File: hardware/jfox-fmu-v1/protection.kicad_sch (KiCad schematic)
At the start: 12 parts, among them U40 USBLC6-2SC6

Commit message: Mezzanine to the carrier, microSD on the edge, sensors moved clear
Three placement changes, and the third is now measured rather than asserted.

QUICK ASSEMBLY. Ten JST-GH headers become one 60-way 0.5 mm mezzanine
(DF12C3.0-60DS) to the carrier, which is what ARCHITECTURE.md already argued
for: eleven looms is eleven things to make, inspect and vibrate loose.
Grounds are interleaved between signal groups rather than grouped at one end,
because a 60-pin connector with no local return is the worst discontinuity on
a board.

What deliberately does NOT cross it: the isolated CAN. A 0.5 mm pitch gives
about 0.5 mm of creepage between adjacent contacts, so running CAN1_H/L
alongside board-referenced signals would quietly reduce the isolation barrier
to that gap - which defeats the ISOW1044 entirely. CAN keeps dedicated
connectors on the isolated side. Debug, USB and the card slot also stay on the
module, because they are used at the module: putting them on the carrier means
unbolting the aircraft to read a log.

The three ferrites became one. Every harness now leaves through the mezzanine,
so there is one 5 V feed to filter instead of three - and three ferrites
driving nets nothing connects to is worse than none.

MICROSD ON THE EDGE, aligned by COURTYARD rather than origin. The first
attempt placed it by its origin and hung a 15 mm deep socket off the board.
The card now ejects outward, off the board, not into U10.

SENSORS MOVED, and the reason checked. The mezzanine freed ten headers' worth
of edge, so the sensors get a dedicated island in the bottom-left - the corner
furthest from both the buck at top-left and the isolated converters at
top-right. The magnetometer is placed by hand in the far corner rather than
packed, because DO-160G s15 makes it the most placement-sensitive part here.

check_fmu_placement.py measures it. "Keep the sensors away from the noise" is
obviously right, impossible to argue with, and untestable as written. Each
sensitive part now has a mini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
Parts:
- removed FB2, FB3: 600R@100MHz, Inductor_SMD:L_0805_2012Metric, symbol Device:FerriteBead
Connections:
- net +5V_TELEM renamed +5V_CARRIER
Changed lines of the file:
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@@
 		(instances
 			(project "jfox-fmu"
-				(path "/009937f3-12d8-4eba-91f7-a35ebf6e45f6"
+				(path "/7ec73105-955f-464d-bc9a-bc93cbe93b7f"
 					(reference "D4")
 					(unit 1)
@@
 		(instances
 			(project "jfox-fmu"
-				(path "/009937f3-12d8-4eba-91f7-a35ebf6e45f6"
+				(path "/7ec73105-955f-464d-bc9a-bc93cbe93b7f"
 					(reference "D5")
 					(unit 1)
@@
 		(instances
 			(project "jfox-fmu"
-				(path "/009937f3-12d8-4eba-91f7-a35ebf6e45f6"
+				(path "/7ec73105-955f-464d-bc9a-bc93cbe93b7f"
 					(reference "D6")
 					(unit 1)
@@
 		(instances
 			(project "jfox-fmu"
-				(path "/009937f3-12d8-4eba-91f7-a35ebf6e45f6"
+				(path "/7ec73105-955f-464d-bc9a-bc93cbe93b7f"
 					(reference "U40")
 					(unit 1)
@@
 		(instances
 			(project "jfox-fmu"
-				(path "/009937f3-12d8-4eba-91f7-a35ebf6e45f6"
+				(path "/7ec73105-955f-464d-bc9a-bc93cbe93b7f"
 					(reference "L5")
 					(unit 1)
@@
 		(instances
 			(project "jfox-fmu"
-				(path "/009937f3-12d8-4eba-91f7-a35ebf6e45f6"
+				(path "/7ec73105-955f-464d-bc9a-bc93cbe93b7f"
 					(reference "L3")
 					(unit 1)
@@
 		(instances
 			(project "jfox-fmu"
-				(path "/009937f3-12d8-4eba-91f7-a35ebf6e45f6"
+				(path "/7ec73105-955f-464d-bc9a-bc93cbe93b7f"
 					(reference "D7")
 					(unit 1)
@@
 		(instances
 			(project "jfox-fmu"
-				(path "/009937f3-12d8-4eba-91f7-a35ebf6e45f6"
+				(path "/7ec73105-955f-464d-bc9a-bc93cbe93b7f"
 					(reference "L4")
 					(unit 1)
@@
 		(instances
 			(project "jfox-fmu"
-				(path "/009937f3-12d8-4eba-91f7-a35ebf6e45f6"
+				(path "/7ec73105-955f-464d-bc9a-bc93cbe93b7f"
 					(reference "D8")
 					(unit 1)
@@
 		(instances
 			(project "jfox-fmu"
-				(path "/009937f3-12d8-4eba-91f7-a35ebf6e45f6"
+				(path "/7ec73105-955f-464d-bc9a-bc93cbe93b7f"
 					(reference "FB1")
 					(unit 1)
@@
 		)
 	)
-	(global_label "+5V_TELEM"
+	(global_label "+5V_CARRIER"
 		(shape input)
 		(at 58.42 138.43 180)
 		(fields_autoplaced yes)
 		(effects
-			(font
-				(size 1.27 1.27)
-			)
-			(justify left)
-		)
-	)
-	(symbol
-		(lib_id "Device:FerriteBead")
-		(at 104.14 130.81 0)
-		(unit 1)
-		(exclude_from_sim no)(in_bom yes)(on_board yes)(dnp no)
-		(property "Reference" "FB2"
-			(at 104.14 119.38 0)
-			(effects
-			(font
-				(size 1.27 1.27)
-			)
-		)
-		)
-		(property "Value" "600R@100MHz"
-			(at 104.14 142.24 0)
-			(effects
-			(font
-				(size 1.27 1.27)
-			)
-		)
-		)
-		(property "Footprint" "Inductor_SMD:L_0805_2012Metric"
-			(at 104.14 130.81 0)
-			(hide yes)
-			(effects
-			(font
-				(size 1.27 1.27)
-			)
-		)
-		)
-		(instances
-			(project "jfox-fmu"
-				(path "/009937f3-12d8-4eba-91f7-a35ebf6e45f6"
-					(reference "FB2")
-					(unit 1)
-				)
-			)
-		)
-	)
-	(wire
-		(pts
-			(xy 104.14 127.0) (xy 104.14 123.19)
-		)
-		(stroke
-			(width 0)
-			(type default)
-		)
-	)
-	(global_label "+5V"
-		(shape input)
-		(at 104.14 123.19 180)
-		(fields_autoplaced yes)
-		(effects
-			(font
-				(size 1.27 1.27)
-			)
-			(justify left)
-		)
-	)
-	(wire
-		(pts
-			(xy 104.14 134.62) (xy 104.14 138.43)
-		)
-		(stroke
-			(width 0)
-			(type default)
-		)
-	)
-	(global_label "+5V_GPS"
-		(shape input)
-		(at 104.14 138.43 180)
-		(fields_autoplaced yes)
-		(effects
-			(font
-				(size 1.27 1.27)
-			)
-			(justify left)
-		)
-	)
-	(symbol
-		(lib_id "Device:FerriteBead")
-		(at 149.86 130.81 0)
-		(unit 1)
-		(exclude_from_sim no)(in_bom yes)(on_board yes)(dnp no)
-		(property "Reference" "FB3"
-			(at 149.86 119.38 0)
-			(effects
-			(font
-				(size 1.27 1.27)
-			)
-		)
-		)
-		(property "Value" "600R@100MHz"
-			(at 149.86 142.24 0)
-			(effects
-			(font
-				(size 1.27 1.27)
-			)
-		)
-		)
-		(property "Footprint" "Inductor_SMD:L_0805_2012Metric"
-			(at 149.86 130.81 0)
-			(hide yes)
-			(effects
-			(font
-				(size 1.27 1.27)
-			)
-		)
-		)
-		(instances
-			(project "jfox-fmu"
-				(path "/009937f3-12d8-4eba-91f7-a35ebf6e45f6"
-					(reference "FB3")
-					(unit 1)
-				)
-			)
-		)
-	)
-	(wire
-		(pts
-			(xy 149.86 127.0) (xy 149.86 123.19)
-		)
-		(stroke
-			(width 0)
-			(type default)
-		)
-	)
-	(global_label "+5V"
-		(shape input)
-		(at 149.86 123.19 180)
-		(fields_autoplaced yes)
-		(effects
-			(font
-				(size 1.27 1.27)
-			)
-			(justify left)
-		)
-	)
-	(wire
-		(pts
-			(xy 149.86 134.62) (xy 149.86 138.43)
-		)
-		(stroke
-			(width 0)
-			(type default)
-		)
-	)
-	(global_label "+5V_RC"
-		(shape input)
-		(at 149.86 138.43 180)
-		(fields_autoplaced yes)
-		(effects

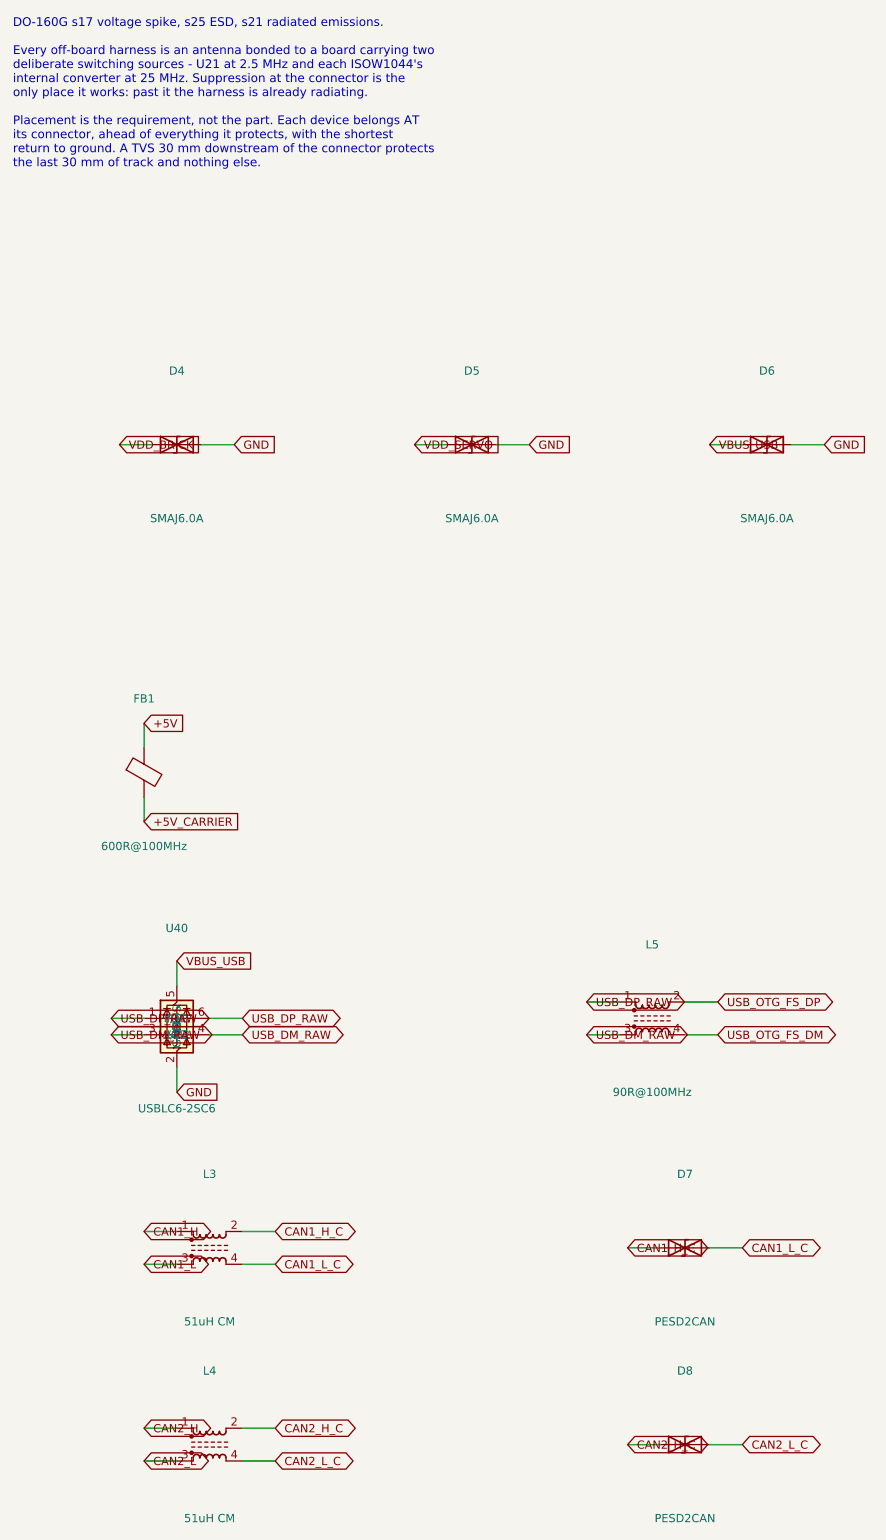
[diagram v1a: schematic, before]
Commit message: Card-cage TMR: FCU becomes a plug-in card, backplane carries the I/O
The FMU stops being a module that mates face-to-face with a base board
underneath it and becomes a card that slides into a backplane. That change
came from the JFOX FCU V1 sketch, and it dissolved a constraint I had
worked around rather than removed: the DF12 mezzanine's 3.0 mm stack height
joins two adjacent boards only, so three channels each needing an
independent path to one base board could not use it. Riser cards were the
workaround. Mating at the card's rear edge means nothing has to span the
gap, so the risers and their extra mated pair per channel are gone.

FCU card, 40 x 90 mm (was 100 x 80):
  * 58-contact Samtec MECF-30 card edge, polarised. Contacts 21/22 are a
    1.24 x 7.0 mm key notch offset from centre - a card the wrong way round
    physically will not enter, which is the only insertion safeguard that
    works before power is applied. Two grounds were sacrificed for it out of
    twenty rather than any signal.
  * Power input tree (LTC4417, six ORing FETs, dividers, input TVS) and the
    debug header move to the backplane. The card receives an already-ORed,
    already-fused +5V_CARRIER on three fingers.
  * Front edge carries everything a person touches: microSD, USB-C, and two
    lamps flanking it. D1 is hardwired to the rail so it lights with no
    firmware running - a power lamp the MCU drives tells you the MCU is
    alive, which is not what anyone reads it for.
  * Power and isolated blocks moved to the back face. Both noise groups are
    grouped at one end so the sensor island can sit 22 mm clear at the
    other; spread out, every point on an 80 mm body is within 13 mm of
    something switching.

JFOX-BASE-v1 backplane, 100 x 100 mm, new:
  * Three independent card-edge sockets in a column. A bent contact in one
    slot costs one channel; a shared bus would cost all three and leave the
    voter nothing to vote on.
  * Two airframe feeds at opposite corners, ORed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
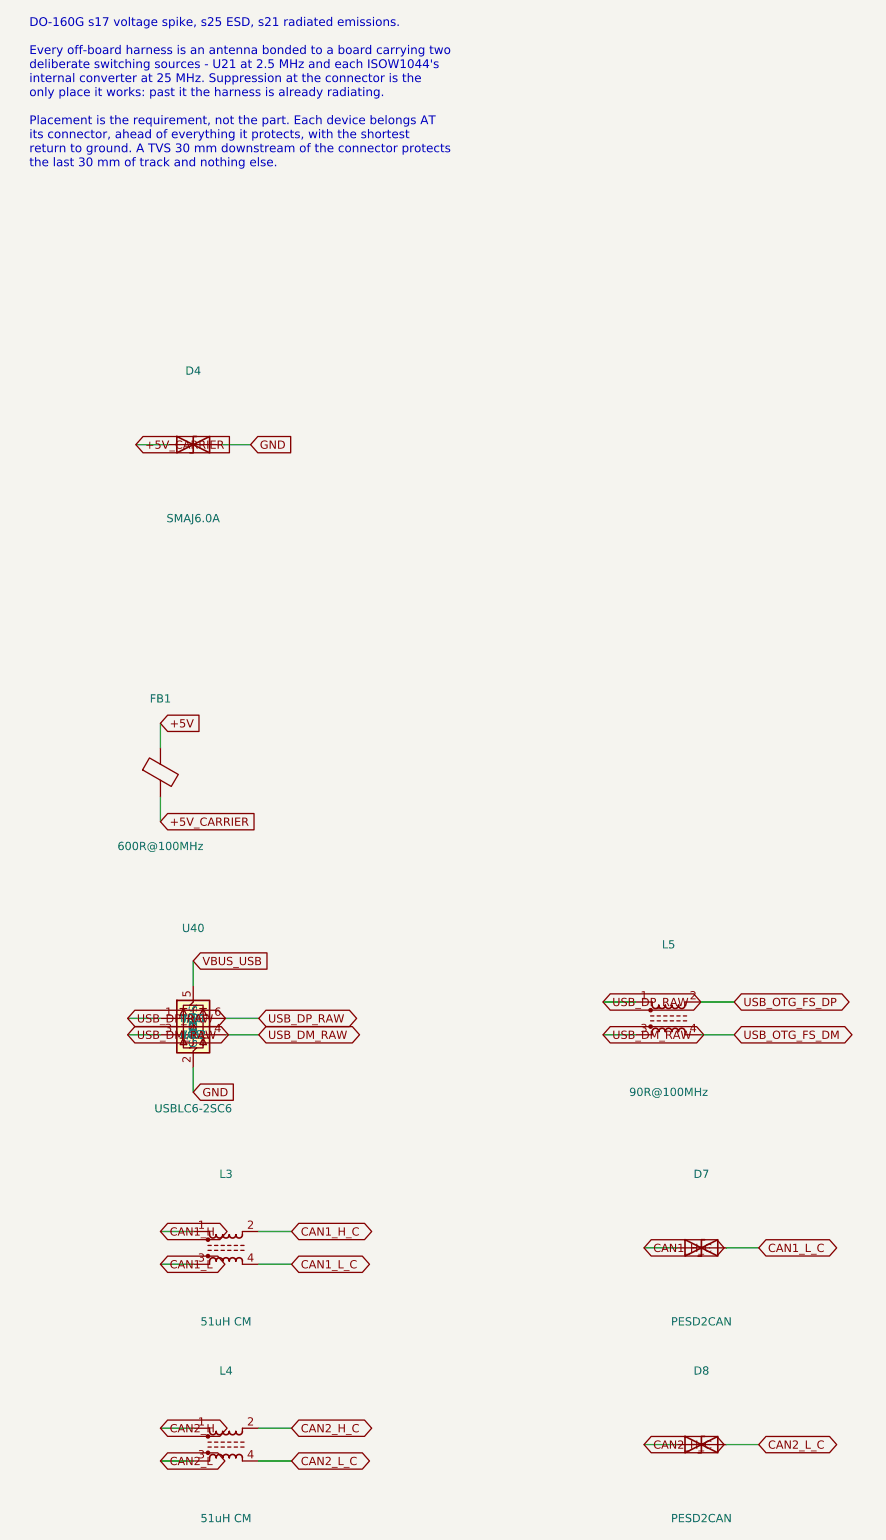
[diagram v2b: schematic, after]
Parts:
- removed D5, D6: SMAJ6.0A, Diode_SMD:D_SMA, symbol Device:D_TVS
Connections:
- net VDD_BRICK is gone; now on net +5V_CARRIER: D4.1 (A1)
